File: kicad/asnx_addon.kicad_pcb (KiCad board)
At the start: 2 copper layers, 61.5 x 43.4 mm, 10 parts, among them J1 OWI1, J2 OWI2, J4 TWI1, J5 TWI2, J7 COM/GPIO, J8 ADC/GPIO

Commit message: Added initial PCB design (incl. BOM)
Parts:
- removed H1, H2, H3, H4: MountingHole, MountingHole:MountingHole_2.7mm_M2.5
- removed the J1 at (175.0, 86.6)
- removed J5: TWI2, Connector_PinHeader_2.54mm:PinHeader_1x04_P2.54mm_Vertical
- added C1: 100n, Capacitor_SMD:C_0603_1608Metric, F.Cu at (124.8, 98.9)
- added C2: 100n, Capacitor_SMD:C_0603_1608Metric, F.Cu at (124.8, 104.6)
- added C3: 100n, Capacitor_SMD:C_0603_1608Metric, F.Cu at (124.8, 111.2)
- added C4: 100n, Capacitor_SMD:C_0603_1608Metric, F.Cu at (124.8, 113.0)
- added JP1: EN_SHT, Jumper:SolderJumper-2_P1.3mm_Bridged_RoundedPad1.0x1.5mm, F.Cu at (131.4, 100.5)
- added JP2: EN_ZMOD, Jumper:SolderJumper-2_P1.3mm_Bridged_RoundedPad1.0x1.5mm, F.Cu at (131.4, 105.5)
- added JP3: EN_BH, Jumper:SolderJumper-2_P1.3mm_Bridged_RoundedPad1.0x1.5mm, F.Cu at (131.4, 110.5)
- added R1: 4k7, Resistor_SMD:R_0603_1608Metric, F.Cu at (124.8, 106.4)
- added U1: SHT30-DIS, my_footprints:Sensirion_DFN-8-1EP_2.5x2.5mm_P0.5mm_EP1.1x1.7mm, F.Cu at (118.8, 98.9)
- added U2: ZMOD4410, my_footprints:ZMOD4410-12-LGA, F.Cu at (118.8, 105.5)
- added U3: BH1750FVI, my_footprints:BH1750FVI-WSOF6I, F.Cu at (118.8, 112.0)
- J2: value OWI2 -> COM/GPIO; footprint Connector_PinHeader_2.54mm:PinHeader_1x03_P2.54mm_Vertical -> Connector_PinHeader_2.54mm:PinHeader_1x14_P2.54mm_Vertical; moved to F.Cu
- J4: value TWI1 -> ADC/GPIO; footprint Connector_PinHeader_2.54mm:PinHeader_1x04_P2.54mm_Vertical -> Connector_PinHeader_2.54mm:PinHeader_1x14_P2.54mm_Vertical; moved to F.Cu
- moved J4 57.1 mm to (118.6, 120.4)
- moved J2 41.1 mm to (151.6, 90.6), turned to 270 degrees
- renumbered J7 to J1, J8 to J3
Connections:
- J1 pad 1: (no net) -> /PC5
- J1 pad 10: (no net) -> /SPI_MOSI
- J1 pad 11: (no net) -> /RXD1
- J1 pad 12: (no net) -> /TXD1
- J1 pad 13: (no net) -> /RESET
- J1 pad 2: (no net) -> /PC4
- J1 pad 3: (no net) -> /PC3
- J1 pad 4: (no net) -> /PC2
- J1 pad 8: (no net) -> /SPI_SCK
- J1 pad 9: (no net) -> /SPI_MISO
- J2 pad 1: +3V3 -> /PC5
- J2 pad 2: GND -> /PC4
- J2 pad 3: (no net) -> /PC3
- J3 pad 10: (no net) -> /PB0
- J3 pad 11: (no net) -> /PB1
- J3 pad 12: (no net) -> /PB2
- J3 pad 13: (no net) -> /PB3
- J3 pad 14: (no net) -> /PB4
- J3 pad 2: (no net) -> /ADC7
- J3 pad 3: (no net) -> /ADC6
- J3 pad 4: (no net) -> /ADC5
- J3 pad 5: (no net) -> /ADC4
- J3 pad 6: (no net) -> /ADC3
- J3 pad 7: (no net) -> /ADC2
- J4 pad 1: +3V3 -> GND
- J4 pad 2: GND -> /ADC7
- J4 pad 3: /I2C_SDA -> /ADC6
- J4 pad 4: /I2C_SCL -> /ADC5
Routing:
- net +3V3: track 0.69 -> 54.0 mm
- net /PC5: track 0.00 -> 52.9 mm, vias 0 -> 2
- net /I2C_SCL: track 0.00 -> 49.8 mm, vias 0 -> 4
- net /PC4: track 0.00 -> 49.1 mm, vias 0 -> 3
- net /I2C_SDA: track 0.00 -> 47.7 mm, vias 0 -> 2
- net /PC3: track 0.00 -> 39.0 mm, vias 0 -> 2
- net /PC2: track 0.00 -> 33.4 mm, vias 0 -> 2
- net /ZMOD_PWR: track 0.00 -> 23.4 mm, vias 0 -> 2
- net /BH_PWR: track 0.00 -> 17.6 mm
- net /SHT_PWR: track 0.00 -> 16.9 mm
- net GND: track 0.00 -> 11.6 mm, vias 0 -> 29
- net /SPI_SCK: track 0.00 -> 4.17 mm
- net /SPI_MISO: track 0.00 -> 4.17 mm
- net /PB0: track 0.00 -> 4.08 mm
- net /PB4: track 0.00 -> 4.06 mm
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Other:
- board size 61.5 x 43.4 mm -> 38.8 x 43.4 mm
- board text added: "2022-02"
- board text added: "BH"
- board text added: "Environmental Monitoring"
- board text added: "SHT"
- board text added: "ZMOD"
- board text removed: "2021-07"
- board text removed: "OWI1"
- board text removed: "OWI2"
- board text removed: "TWI1"
- board text removed: "TWI2"

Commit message: Refined EM addon and added BOM
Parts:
- turned U2 to 180 degrees
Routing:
- net +3V3: track 54.0 -> 67.8 mm
- net GND: vias 29 -> 32

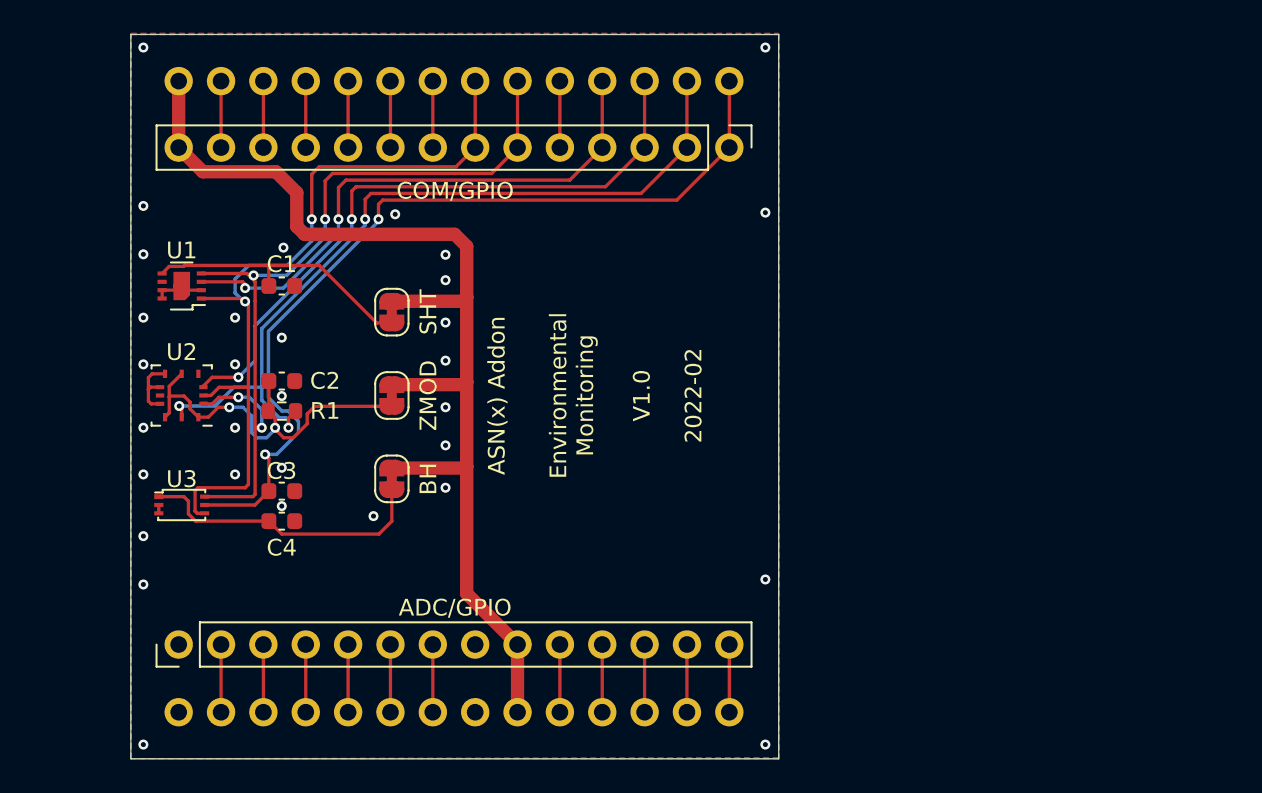
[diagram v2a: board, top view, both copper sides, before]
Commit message: Updated environmental monitoring addon and related information
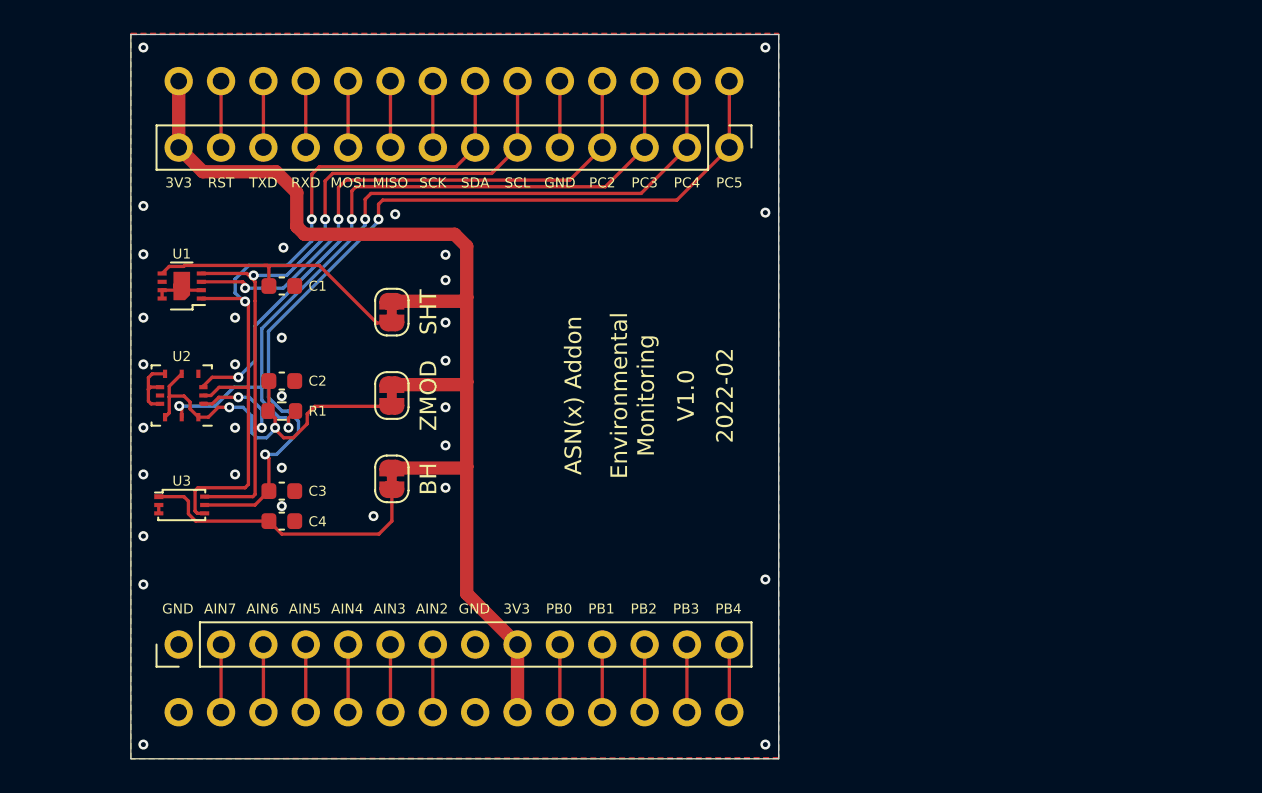
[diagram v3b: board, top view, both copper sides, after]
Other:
- board text added: "3V3"
- board text added: "AIN2"
- board text added: "AIN3"
- board text added: "AIN4"
- board text added: "AIN5"
- board text added: "AIN6"
- board text added: "AIN7"
- board text added: "GND"
- board text added: "MISO"
- board text added: "MOSI"
- board text added: "PB0"
- board text added: "PB1"
- board text added: "PB2"
- board text added: "PB3"
- board text added: "PB4"
- board text added: "PC2"
- board text added: "PC3"
- board text added: "PC4"
- board text added: "PC5"
- board text added: "RST"
- board text added: "RXD"
- board text added: "SCK"
- board text added: "SCL"
- board text added: "SDA"
- board text added: "TXD"
- board text removed: "ADC/GPIO"
- board text removed: "COM/GPIO"
